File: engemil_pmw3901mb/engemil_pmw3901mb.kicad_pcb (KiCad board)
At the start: 2 copper layers, 16 parts, among them J1 6130XX11121, U1 PMW3901MB-TXQT, U2 TLV77333PDBVR, U3 TLV77318PDBVR

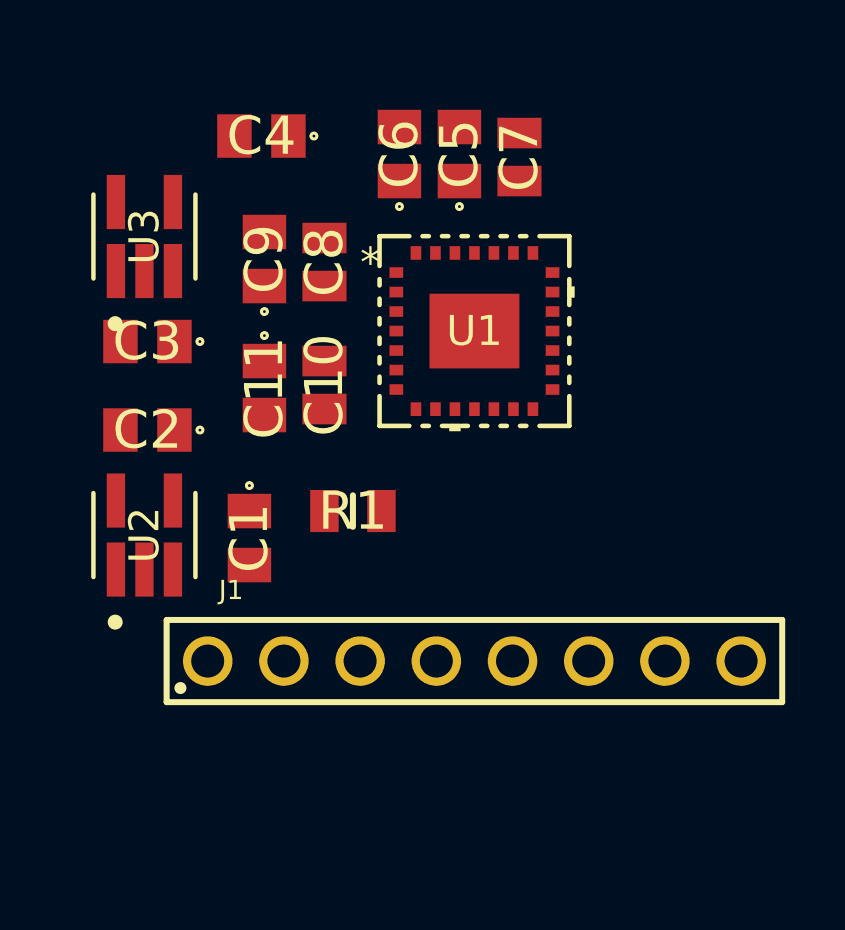
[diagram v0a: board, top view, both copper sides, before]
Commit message: - Updated notes in schematic - Updated PMW3901MB NCS pin fron not connected to unspecified - Updated component orientation in PCB editor
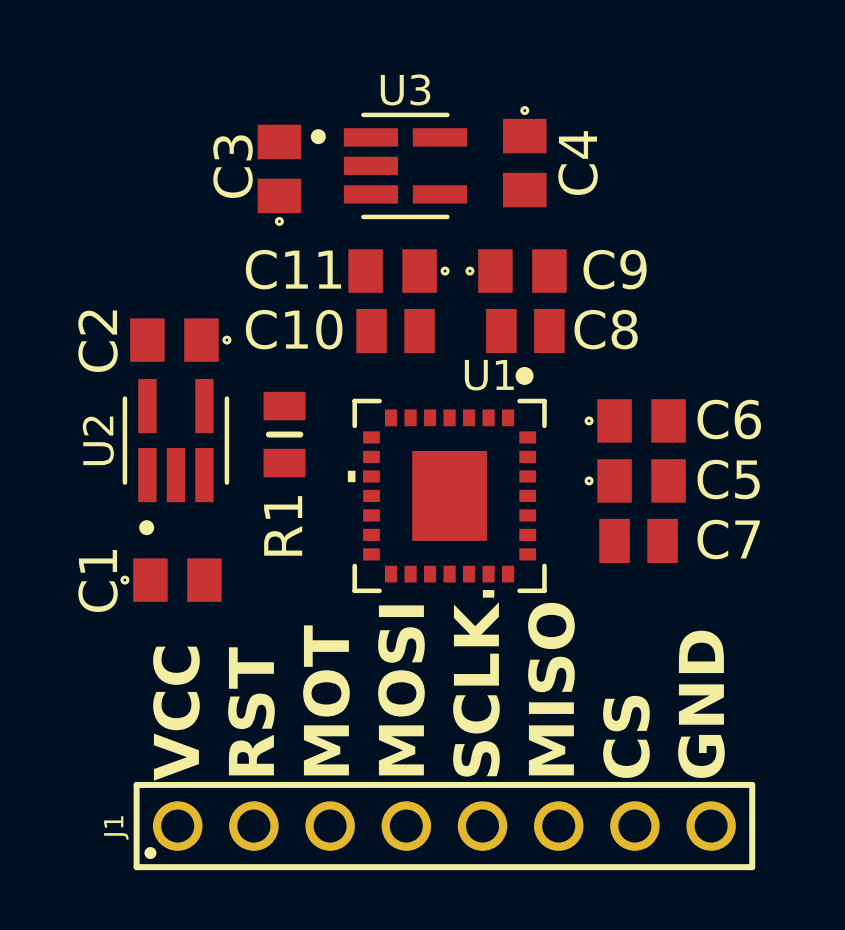
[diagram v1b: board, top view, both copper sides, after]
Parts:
- U1: footprint engemil_pmw3901mb_module_footprint_library:QFN_01MB-TXQT_PIX -> engemil_pmw3901mb_module_footprint_library:QFN_01MB-TXQT_PIX-M
- moved C7 13.4 mm to (156.0, 117.0), turned to 0 degrees
- moved C5 12.5 mm to (156.1, 115.0), turned to 0 degrees
- moved C6 12.0 mm to (156.1, 113.0), turned to 0 degrees
- moved U3 9.01 mm to (148.2, 104.5), turned to 0 degrees
- moved C4 8.82 mm to (152.2, 104.4), turned to -90 degrees
- moved C9 8.61 mm to (152.1, 108.0), turned to 0 degrees
- moved C3 7.24 mm to (144.0, 104.6), turned to 90 degrees
- moved C8 7.08 mm to (152.2, 110.0), turned to 0 degrees
- moved C11 5.78 mm to (147.8, 108.0), turned to 180 degrees
- moved J1 5.59 mm to (149.5, 126.5)
- moved U1 5.56 mm to (149.7, 115.5), turned to -90 degrees
- moved R1 3.42 mm to (144.2, 113.5), turned to -90 degrees
- moved U2 3.32 mm to (140.5, 113.7)
- moved C2 3.13 mm to (140.5, 110.3)
- moved C10 2.98 mm to (147.9, 110.0), turned to 180 degrees
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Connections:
- J1 pad 2: SCLK -> RESET
- J1 pad 3: MISO -> MOTION
- J1 pad 5: CS -> SCLK
- J1 pad 6: MOTION -> MISO
- J1 pad 7: RESET -> CS
- U1 pad 19: unconnected-(U1-NCS-Pad19) -> CS
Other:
- board text added: "CS"
- board text added: "GND"
- board text added: "MISO"
- board text added: "MOSI"
- board text added: "MOT"
- board text added: "RST"
- board text added: "SCLK"
- board text added: "VCC"

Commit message: Updated schematic and pcb
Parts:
- moved U3 2.10 mm to (150.0, 103.5)
- moved C4 1.99 mm to (154.0, 103.6), turned to 90 degrees
- moved C11 1.99 mm to (149.6, 107.2)
- moved C3 1.99 mm to (145.8, 103.8)
- moved C9 1.99 mm to (153.9, 107.2)
- moved C8 1.89 mm to (154.0, 109.5)
- moved C10 1.70 mm to (149.5, 109.5)
- moved C2 1.43 mm to (141.1, 109.0)
- moved C7 1.15 mm to (156.5, 118.0)
- moved J1 1.05 mm to (149.8, 127.5)
- moved C1 0.78 mm to (141.2, 117.8), turned to 180 degrees
- moved U2 0.78 mm to (141.1, 113.2)
- moved C5 0.73 mm to (156.6, 115.5)
- moved R1 0.60 mm to (144.5, 113.0)
- moved U1 0.60 mm to (150.0, 115.0)
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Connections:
- U1 pad 22: unconnected-(U1-NC-Pad22) -> GND
- U1 pad 23: unconnected-(U1-NC-Pad23) -> GND
- U1 pad 24: unconnected-(U1-NC-Pad24) -> GND
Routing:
- net +3.3V: track 0.00 -> 42.1 mm
- net +1V8: track 0.00 -> 26.2 mm
- net VCC: track 0.00 -> 19.0 mm
- net RESET: track 0.00 -> 18.5 mm
- net GND: track 0.00 -> 18.0 mm, vias 0 -> 4
- net CS: track 0.00 -> 12.2 mm
- net MISO: track 0.00 -> 11.4 mm
- net MOTION: track 0.00 -> 10.8 mm
- net SCLK: track 0.00 -> 10.6 mm
- net MOSI: track 0.00 -> 9.96 mm
- net Net-(U1-VREG): track 0.00 -> 5.40 mm
- added copper zone on B.Cu, net GND
- added copper zone on F.Cu, net GND
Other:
- board outline added: 50 x 30 mm

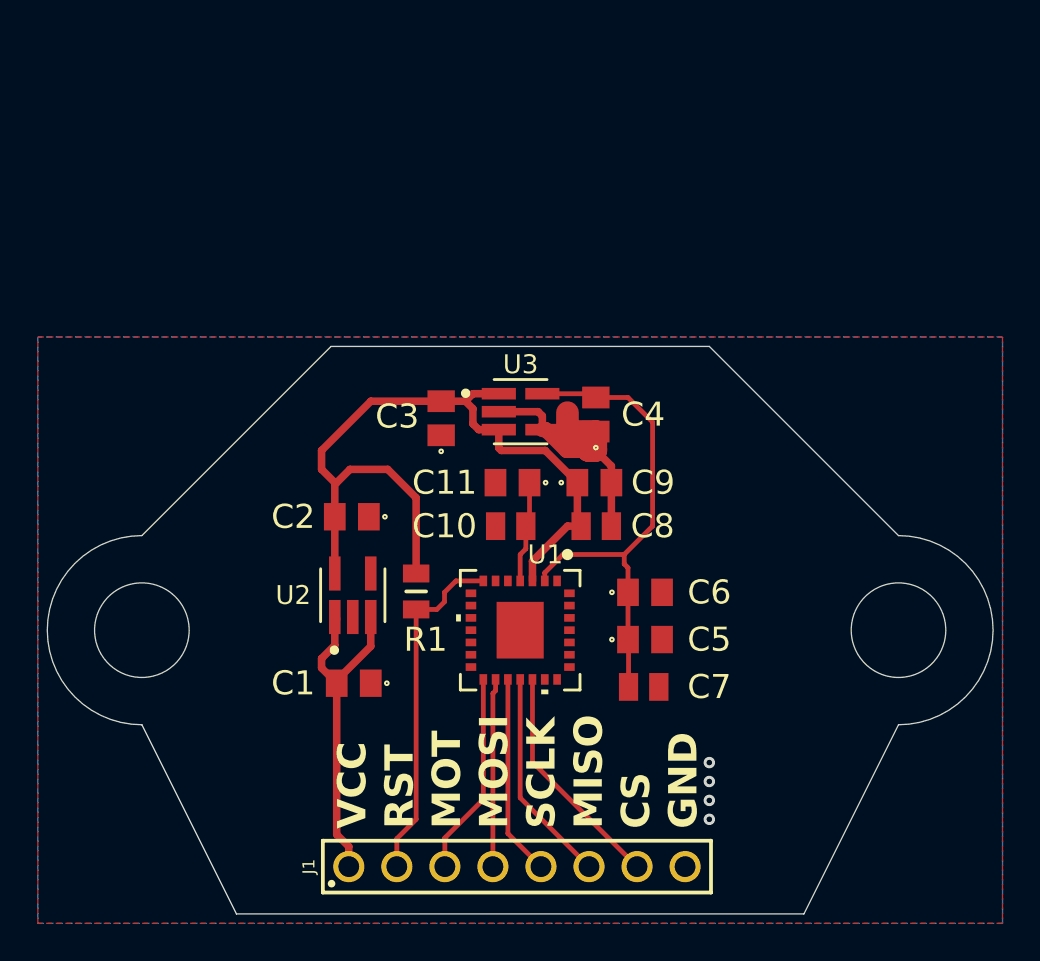
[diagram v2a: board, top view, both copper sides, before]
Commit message: - Added mounting holes in Schematic and PCB - Finished traces and top and bottom ground plains - Added vias for copper islands / isolated copper - Generated pdf of schematic and pcb - Updated README with 3D model
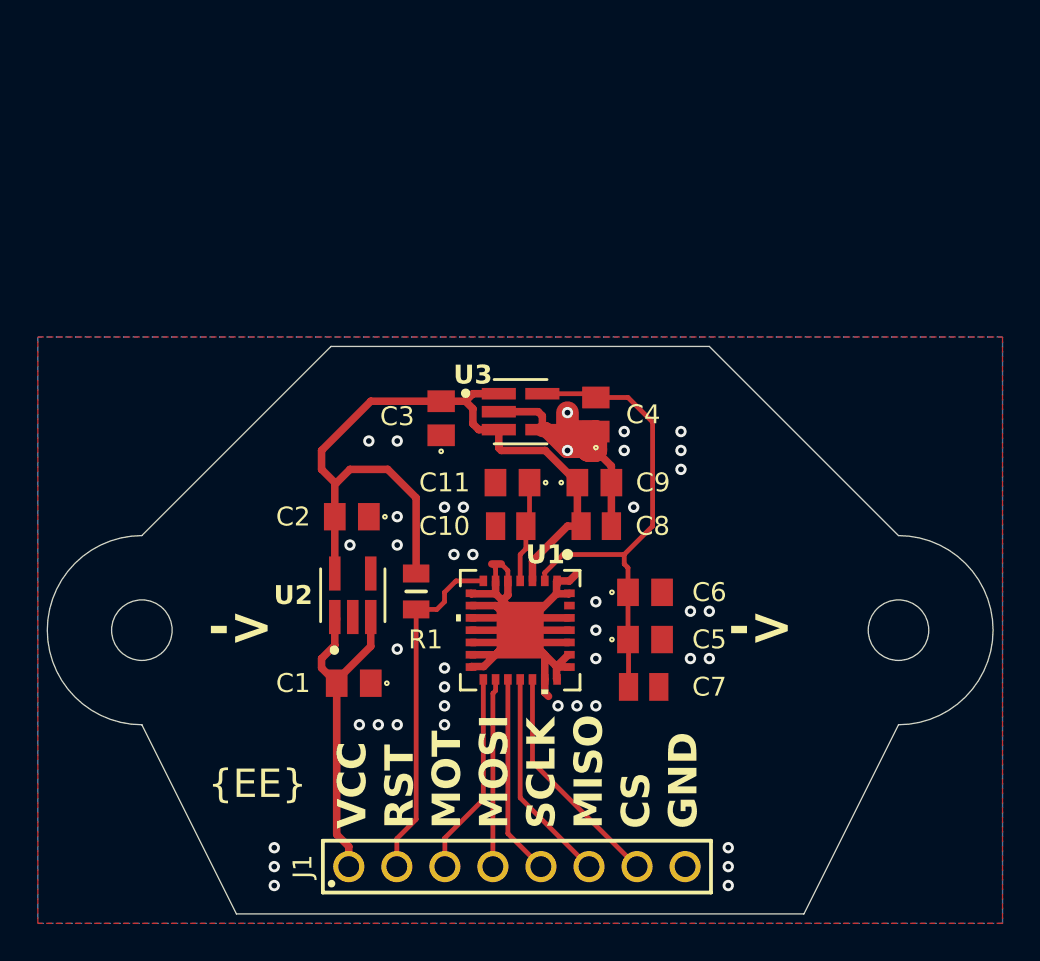
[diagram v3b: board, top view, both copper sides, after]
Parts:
- added H1: MountingHole, MountingHole:MountingHole_3.2mm_M3_ISO14580, F.Cu at (130.0, 115.0)
- added H2: MountingHole, MountingHole:MountingHole_3.2mm_M3_ISO14580, F.Cu at (170.0, 115.0)
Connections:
- U1 pad 1: Net-(U1-GND-Pad1) -> GND
- U1 pad 10: unconnected-(U1-NC-Pad10) -> GND
- U1 pad 11: unconnected-(U1-NC-Pad11) -> GND
- U1 pad 12: unconnected-(U1-NC-Pad12) -> GND
- U1 pad 13: unconnected-(U1-NC-Pad13) -> GND
- U1 pad 14: unconnected-(U1-NC-Pad14) -> GND
- U1 pad 20: unconnected-(U1-NC-Pad20) -> GND
- U1 pad 21: Net-(U1-GND-Pad1) -> GND
- U1 pad 25: unconnected-(U1-NC-Pad25) -> GND
- U1 pad 26: unconnected-(U1-NC-Pad26) -> GND
- U1 pad 27: unconnected-(U1-NC-Pad27) -> GND
- U1 pad 28: unconnected-(U1-NC-Pad28) -> GND
- U1 pad 29: Net-(U1-GND-Pad1) -> GND
- U1 pad 5: unconnected-(U1-NC-Pad5) -> GND
- U1 pad 6: unconnected-(U1-NC-Pad6) -> GND
- U1 pad 8: unconnected-(U1-NC-Pad8) -> GND
- U1 pad 9: unconnected-(U1-NC-Pad9) -> GND
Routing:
- net GND: track 18.0 -> 67.0 mm, vias 4 -> 41
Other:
- outline, holes or cut-outs redrawn
- board text added: "->"
- board text added: "Designed by EngEmil.io {EE}"
- board text added: "EngEmil PMW3901MB v1.0"
- board text added: "{EE}"

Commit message: - Added gerber files - Updated text on bottom silk layer - Updated images for readme file - Updated PCB PDF file
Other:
- board text added: "Optical Flow Sensor Module"
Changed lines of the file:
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@@
 			(outputformat 1)
 			(mirror no)
-			(drillshape 1)
+			(drillshape 0)
 			(scaleselection 1)
-			(outputdirectory "")
+			(outputdirectory "../gerbers/")
 		)
 	)
@@
 		)
 	)
+	(gr_text "Optical Flow Sensor Module"
+		(at 165.5 112 0)
+		(layer "B.SilkS")
+		(effects
+			(font
+				(size 1.5 1.5)
+				(thickness 0.2)
+			)
+			(justify left bottom mirror)
+		)
+	)

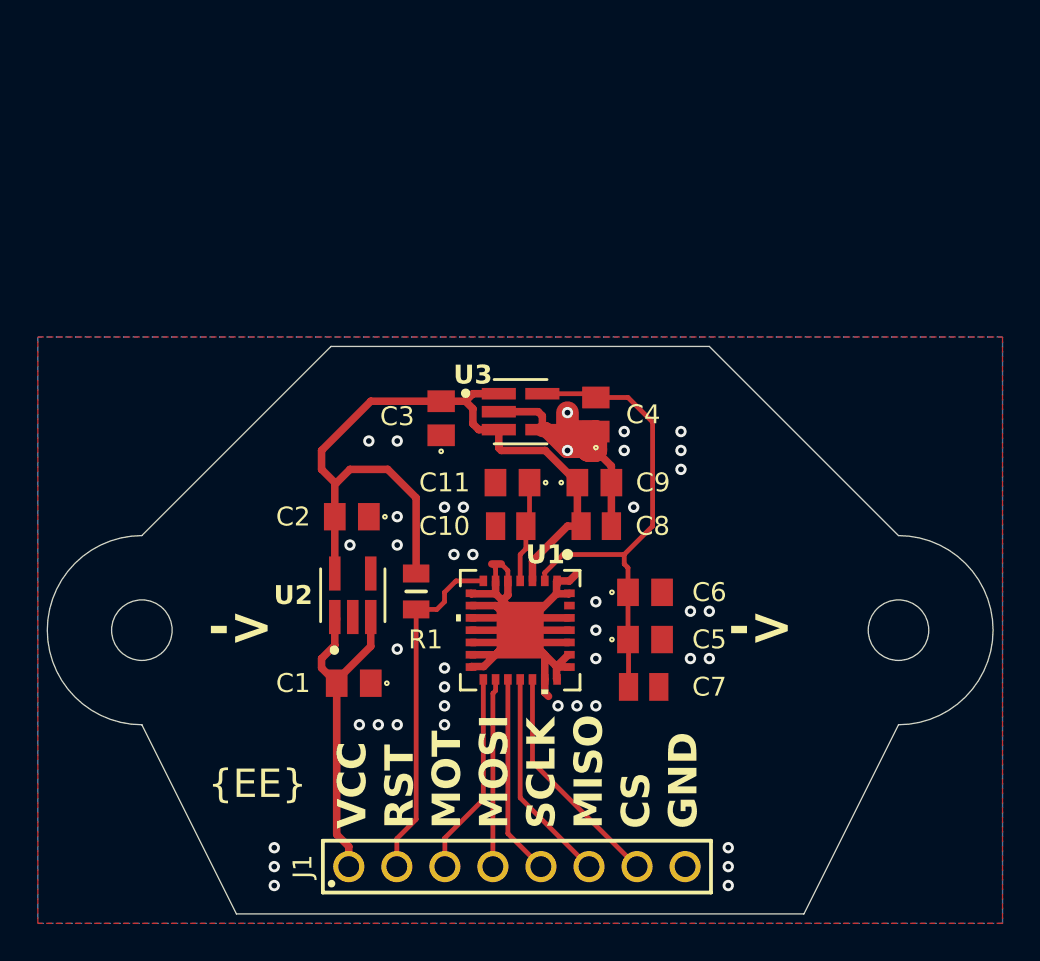
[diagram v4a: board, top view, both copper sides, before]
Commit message: - Removed 3v3 voltage regulator and two capacitors - Changed reference designators (C1,C2,...,U2,U3,...) - Added R4 - Marked C3 and C4 as not mount - Added comment about RC filter - Added pull-up resistors for SCLK and MISO - Marked R2 and R3 as not mount - Added notes for 8-pin connector - Added ESD protection diodes - Updated BOM - Removed zip file in raw folder (unused and not imported) - Added datasheets for components under docs folder - Imported new components into project - Updated schematic version and date - Generated new schematic pdf - Started on redesigning pcb layout (work-in-progress)
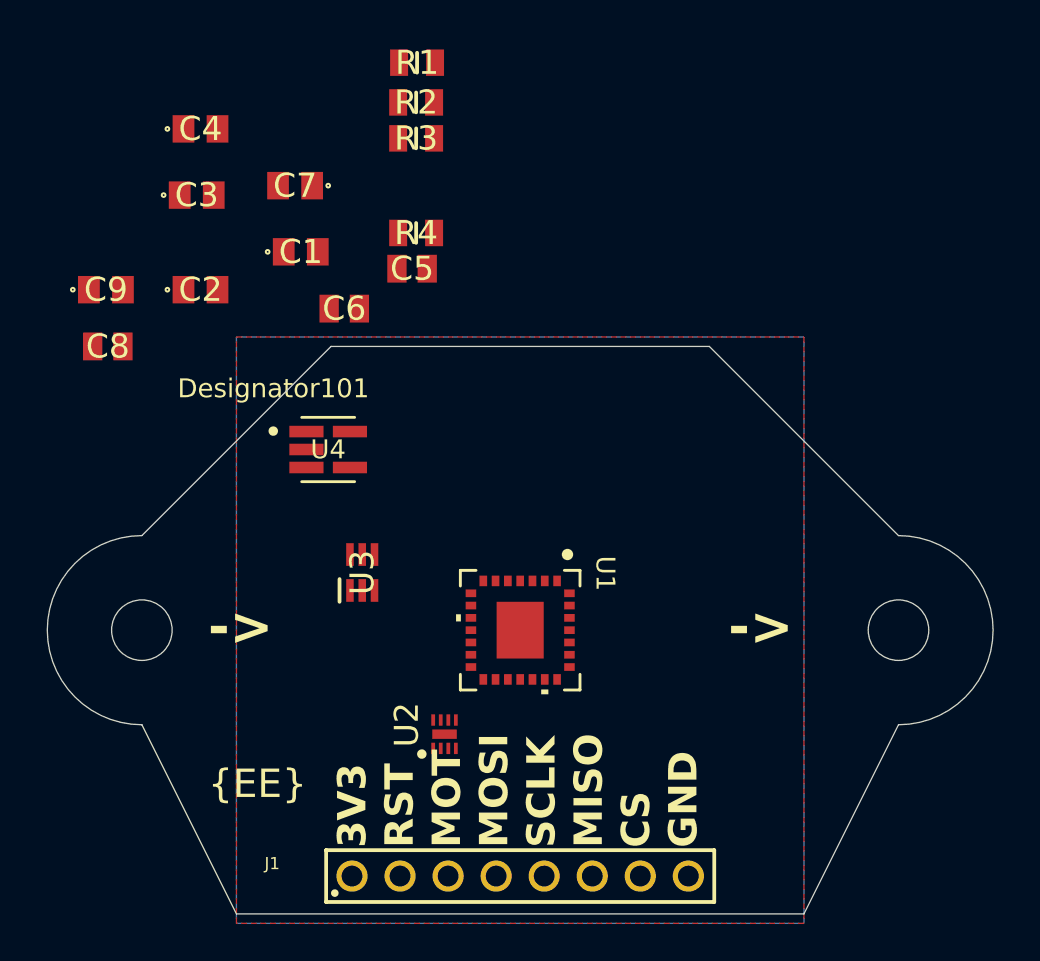
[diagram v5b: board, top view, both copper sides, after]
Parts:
- removed C10: 0.1uF, engemil_pmw3901mb_module_footprint_library:CAPC2012X110N
- removed C11: 4.7uF, engemil_pmw3901mb_module_footprint_library:C0805
- added R2: Not Mount, engemil_pmw3901mb_module_footprint_library:RESC2012X60N, F.Cu at (144.5, 87.1)
- added R3: Not Mount, engemil_pmw3901mb_module_footprint_library:RESC2012X60N, F.Cu at (144.5, 89.0)
- added R4: 0Ohm, engemil_pmw3901mb_module_footprint_library:RESC2012X60N, F.Cu at (144.5, 94.0)
- added U4: TLV77318PDBVR, engemil_pmw3901mb_module_footprint_library:DBV0005A-IPC_A, F.Cu at (139.8, 105.5)
- C3, C4: value 1uF -> Not Mount
- C5, C6: value 22uF -> 0.1uF; footprint engemil_pmw3901mb_module_footprint_library:C0805 -> engemil_pmw3901mb_module_footprint_library:CAPC2012X110N
- C7: value 0.1uF -> 10uF; footprint engemil_pmw3901mb_module_footprint_library:CAPC2012X110N -> engemil_pmw3901mb_module_footprint_library:C0805
- C9: value 10uF -> 4.7uF
- U2: value TLV77333PDBVR -> TPD8E003DQDR; footprint engemil_pmw3901mb_module_footprint_library:DBV0005A-IPC_A -> engemil_pmw3901mb_module_footprint_library:SON40P135X170X80-9N
- U3: value TLV77318PDBVR -> LM66100QDCKRQ1; footprint engemil_pmw3901mb_module_footprint_library:DBV0005A-IPC_A -> engemil_pmw3901mb_module_footprint_library:SOT65P210X110-6N
- moved C7 32.3 mm to (138.1, 91.5), turned to 180 degrees
- moved R1 28.0 mm to (144.6, 85.0), turned to 0 degrees
- moved C9 27.8 mm to (128.1, 97.0)
- moved C8 27.5 mm to (128.2, 100.0)
- moved C4 25.8 mm to (133.1, 88.5), turned to 0 degrees
- moved C5 23.2 mm to (144.3, 95.9)
- moved C1 23.0 mm to (138.4, 95.0), turned to 0 degrees
- moved C6 21.9 mm to (140.7, 98.0)
- moved C3 17.5 mm to (132.9, 92.0), turned to 0 degrees
- moved C2 14.4 mm to (133.1, 97.0), turned to 0 degrees
- moved U3 11.9 mm to (141.7, 112.0), turned to 90 degrees
- moved U2 8.80 mm to (146.0, 120.5)
- moved J1 0.53 mm to (150.0, 128.0)
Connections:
- C1 pad 2: VCC -> +3.3V
- C2 pad 2: +3.3V -> +1V8
- C3 pad 1: GND -> Net-(U1-VDD)
- C3 pad 2: +3.3V -> GND
- C4 pad 1: GND -> Net-(U1-VDD)
- C4 pad 2: +1V8 -> GND
- C5 pad 1: +1V8 -> Net-(U1-VDD)
- C6 pad 1: +1V8 -> +3.3V
- C7 pad 1: +1V8 -> +3.3V
- C8 pad 1: +3.3V -> Net-(U1-VREG)
- C9 pad 1: +3.3V -> Net-(U1-VREG)
- U1 pad 1: GND -> Net-(U1-GND-Pad1)
- U1 pad 2: +1V8 -> Net-(U1-VDD)
- U1 pad 20: GND -> Net-(U1-GND-Pad1)
- U1 pad 21: GND -> Net-(U1-GND-Pad1)
- U1 pad 22: GND -> Net-(U1-GND-Pad1)
- U1 pad 23: GND -> Net-(U1-GND-Pad1)
- U1 pad 24: GND -> Net-(U1-GND-Pad1)
- U1 pad 25: GND -> Net-(U1-GND-Pad1)
- U1 pad 26: GND -> Net-(U1-GND-Pad1)
- U1 pad 27: GND -> Net-(U1-GND-Pad1)
- U1 pad 28: GND -> Net-(U1-GND-Pad1)
- U1 pad 29: GND -> Net-(U1-GND-Pad1)
- U2 pad 2: GND -> MOTION
- U2 pad 3: VCC -> SCLK
- U2 pad 4: GND -> CS
- U2 pad 5: +3.3V -> unconnected-(U2-IO5-Pad5)
- U3 pad 1: +3.3V -> VCC
- U3 pad 3: +3.3V -> GND
- U3 pad 5: +1V8 -> GND
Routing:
- net GND: track 67.0 -> 0.00 mm, vias 41 -> 0
- net +3.3V: track 42.1 -> 0.00 mm
- net +1V8: track 26.2 -> 0.00 mm
- net VCC: track 19.0 -> 0.00 mm
- net RESET: track 18.5 -> 0.00 mm
- net CS: track 12.2 -> 0.00 mm
- net MISO: track 11.4 -> 0.00 mm
- net MOTION: track 10.8 -> 0.00 mm
- net SCLK: track 10.6 -> 0.00 mm
- net MOSI: track 9.96 -> 0.00 mm
- net Net-(U1-VREG): track 5.40 -> 0.00 mm
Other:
- board text added: "3V3"
- board text removed: "VCC"
